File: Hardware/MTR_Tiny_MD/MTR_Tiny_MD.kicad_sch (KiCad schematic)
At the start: 82 parts, among them J1 USB_C_Receptacle_USB2.0, J2 68021-412HLF, J3 LED OUT, J4 UART, J5 LED OUT, J6 XT30PB, Q1 AO3401A, SW1 Boot, SW2 Reset, U1 RP2040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

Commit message: add usb C PD controler
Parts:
- removed C17, C22: 10uF, Capacitor_SMD:C_0603_1608Metric, symbol Device:C
- removed F1: 500mA, Fuse:Fuse_0603_1608Metric, symbol Device:Fuse_Small
- removed F2: 250mA, Fuse:Fuse_0603_1608Metric, symbol Device:Fuse_Small
- removed U4: TPS71933-33DRVR, Personal:TPS71933-33DRVR, symbol 2023-01-28_15-38-30:TPS71933-33DRVR
- added 3v3ToVddd1: 3V3toVddJumper, Resistor_SMD:R_0201_0603Metric, symbol Jumper:SolderJumper_2_Open
- added C14, C16, C19, C22, C43: 4.7uF, Capacitor_SMD:C_0402_1005Metric, symbol Device:C_Small
- added C15, C17, C21: 100nF, Capacitor_SMD:C_0402_1005Metric, symbol Device:C_Small
- added C23: DNF, Capacitor_SMD:C_0402_1005Metric, symbol Device:C_Small
- added Coarse1: CurrentSelect, Resistor_SMD:R_0201_0603Metric, symbol Jumper:SolderJumper_2_Open
- added D4: SAFE_MODE, LED_SMD:LED_0603_1608Metric, symbol Device:LED_Small
- added JP7: +5V_SAFE, Resistor_SMD:R_0201_0603Metric, symbol Jumper:SolderJumper_2_Open
- added JP8: +VBUS_OUT, Resistor_SMD:R_0201_0603Metric, symbol Jumper:SolderJumper_2_Open
- added R10, R24: 20k, Resistor_SMD:R_0402_1005Metric, symbol Device:R_Small
- added R17, R26: 2k2, Resistor_SMD:R_0402_1005Metric, symbol Device:R_Small
- added R18: 820R, Resistor_SMD:R_0402_1005Metric, symbol Device:R_Small
- added R22: 1k, Resistor_SMD:R_0402_1005Metric, symbol Device:R_Small
- added R23: 5.1k, Resistor_SMD:R_0402_1005Metric, symbol Device:R_Small
- added U4, U9: SIA931DJ-T1-GE3, footprints:MOSFET_T1-GE3_VIS, symbol 2023-08-24_16-54-04:SIA931DJ-T1-GE3
- added U8: CYPD3177-24LQXQT, CYPD3177-24LQXQT_CYP, symbol 2023-08-24_13-49-11:CYPD3177-24LQXQT
- added Vbus1, VbusSafe1: VbusJumper, Resistor_SMD:R_0201_0603Metric, symbol Jumper:SolderJumper_2_Open
- added VbusMax1: VbusMax, Resistor_SMD:R_0201_0603Metric, symbol Jumper:SolderJumper_2_Open
- added VbusMin1: VbusMin, Resistor_SMD:R_0201_0603Metric, symbol Jumper:SolderJumper_2_Open
- D3: value USB ON -> LED
- H6, H7: footprint TestPoint:TestPoint_Pad_1.5x1.5mm -> TestPoint:TestPoint_Pad_D1.0mm
- J6: footprint Personal:XT30PB -> footprints:CONN_XT30UPB-M_AMA
- R16: value 100R -> 5.1k
- R5: value 1k -> DNF
- SW1, SW2: footprint Personal:TVBM17 -> Button_Switch_additional:TVAF06-A020B-R
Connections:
- net FeedBack is gone; now on net +3V3: C40.1, C41.1, C42.1, L2.2, U7.4 (FB/VOUT)
- net V_USB is gone; now on net GPIO23: J2.3, R12.2
- net +3V3: now also 3v3ToVddd1.1 (A), Coarse1.1 (A), R23.2, VbusMax1.1 (A)
- net ALIM: now also JP7.2 (B), JP8.2 (B)
- net GND: now also C14.2, C15.2, C16.2, C17.2, C19.1, C21.1, D4.1 (K), R22.1, U8.19 (GND), VbusMin1.1 (A); no longer J1.S1 (SHIELD), U5.41 (EPAD)
- net GPIO24: now also J2.9; no longer J2.7
- net GPIO25: now also J2.7; no longer J2.5
- net I2C_SCL: now also U8.13 (HPI_SCL)
- net I2C_SDA: now also U8.12 (HPI_SDA)
- net USB_D+: no longer J1.A6 (D+)
- net USB_D-: no longer J1.A7 (D-)
- net GPIO23: now reaches U1.35 (GPIO23)
- net +VBUS: now reaches J1.A4 (VBUS), J1.A9 (VBUS), J1.B4 (VBUS), J1.B9 (VBUS)
- net +VBUS: now also C19.2, C21.2, U8.18 (VBUS_IN), Vbus1.1 (A), VbusSafe1.1 (A)
- net CC1: now reaches J1.A5 (CC1)
- net CC1: now also U8.15 (CC1)
- net CC2: now reaches J1.B5 (CC2)
- net CC2: now also U8.14 (CC2)
- new net: D4.2 (A), R18.1
- new net +5V_SAFE: JP7.1 (A), R18.2, U4.3 (D2), U4.8 (D2)
- new net +VBUS_FET_EN: R26.1, U8.3 (VBUS_FET_EN)
- new net +VBUS_OUT: C23.1, J2.5, JP8.1 (A), U8.11 (VDC_OUT), U9.3 (D2), U9.8 (D2)
- new net DRAIN_1: C22.1, R24.2, U9.6 (D1), U9.7 (D1), Vbus1.2 (B)
- new net DRAIN_1_SAFE: C43.1, R10.2, U4.6 (D1), U4.7 (D1), VbusSafe1.2 (B)
- new net GATE: C22.2, C23.2, R24.1, R26.2, U9.2 (G1), U9.5 (G2)
- new net GATE_SAFE: C43.2, R10.1, R17.2, U4.2 (G1), U4.5 (G2)
- new net ISNK_COARSE: Coarse1.2 (B), U8.5 (ISNK_COARSE)
- new net ISNK_FINE: R22.2, R23.1, U8.6 (ISNK_FINE)
- new net SAFE_PWR_EN: R17.1, U8.4 (SAFE_PWR_EN)
- new net SOURCE: U9.1 (S1), U9.4 (S2)
- new net SOURCE_SAFE: U4.1 (S1), U4.4 (S2)
- new net VBUS_MAX: U8.2 (VBUS_MAX), VbusMax1.2 (B)
- new net VBUS_MIN: U8.1 (VBUS_MIN), VbusMin1.2 (B)
- new net VCCD: C16.1, U8.24 (VCCD)
- new net VDDD: 3v3ToVddd1.2 (B), C14.1, C15.1, C17.1, U8.23 (VDDD)
- no-connect marks 10 -> 14
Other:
- note added: "DNF - Not on PCB"
- note added: "Fine current +/-250mA"
- note added: "Maximal voltage 20V"
- note added: "Minimun voltage 5V"
- note added: "Nominal current 0-5A"
- note added: "Safe 5V feedback if negociation fail"
- note added: "USB C + Power Delivery"
- note removed: "USB C + Power"
- moved on the sheet: C1, C10, C11, C12, C13, C18, C20, C24, C25, C26, C27, C28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

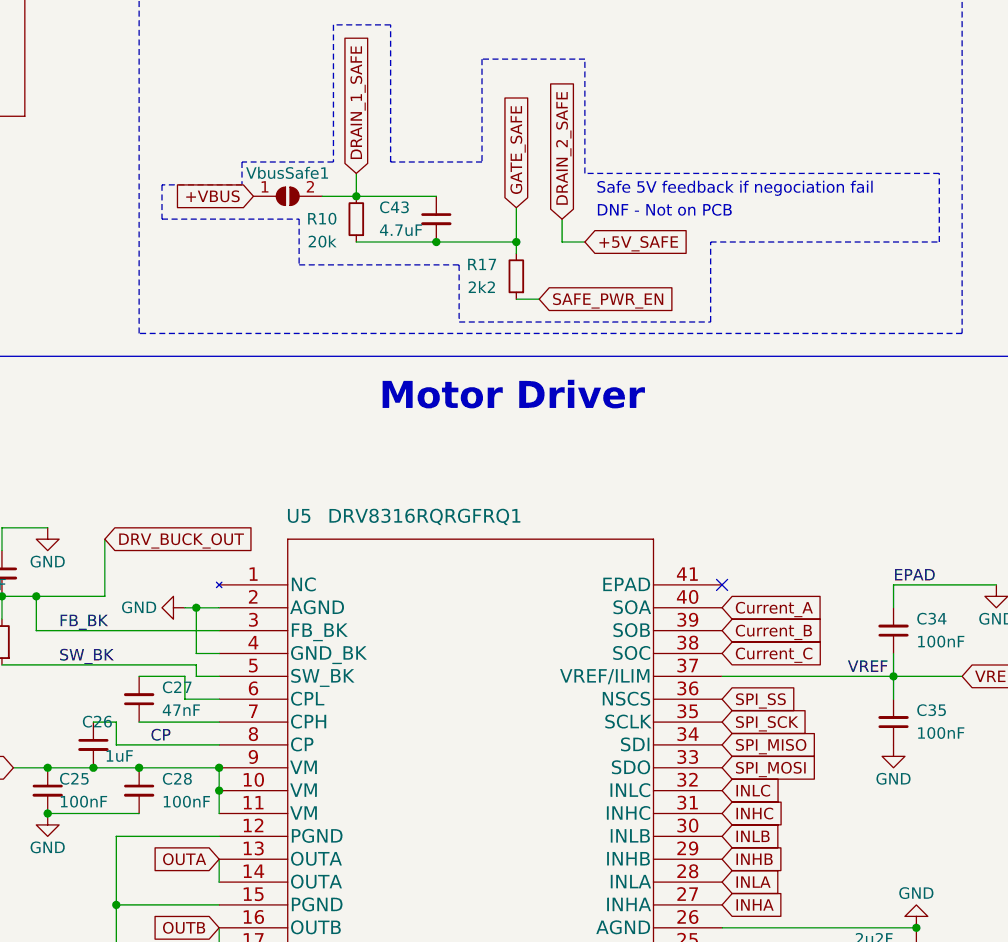
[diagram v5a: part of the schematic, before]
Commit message: Update design, add PD controler, correct SPI
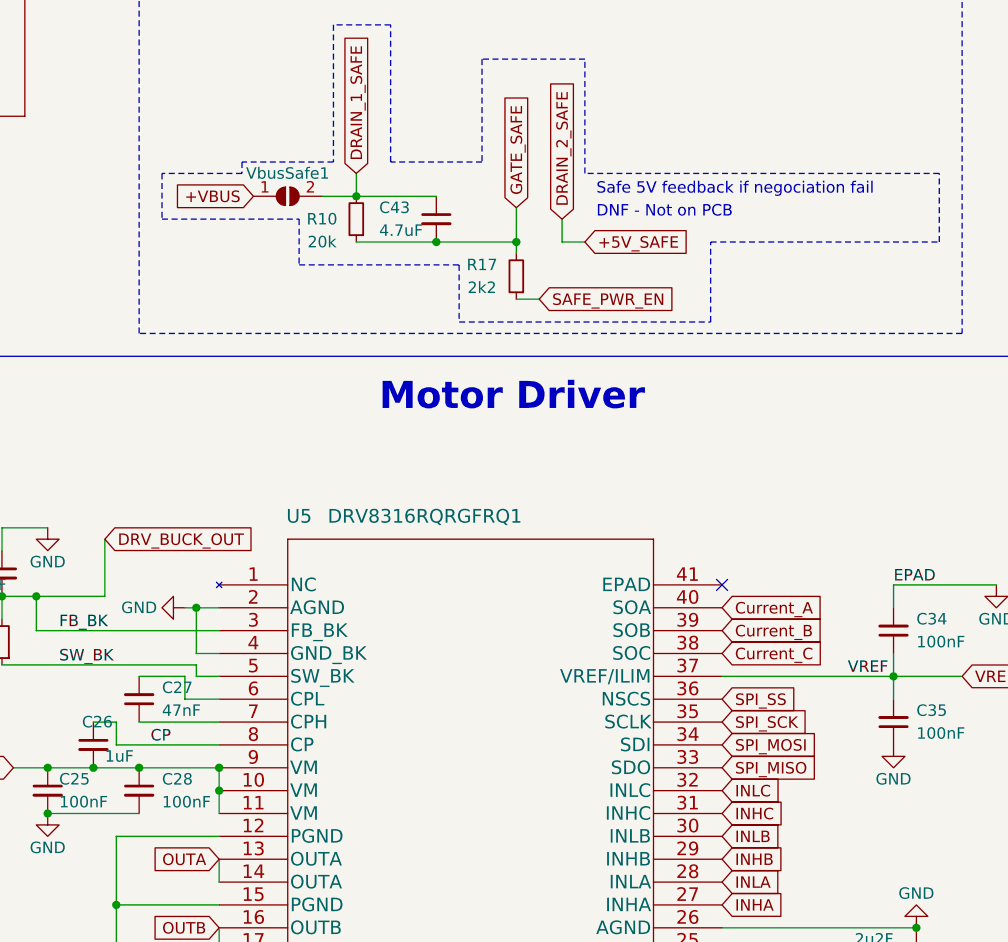
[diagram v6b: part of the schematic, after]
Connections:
- net SPI_MISO: now also U5.33 (SDO); no longer U5.34 (SDI)
- net SPI_MOSI: now also U5.34 (SDI); no longer U5.33 (SDO)

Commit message: Update 1.2.2
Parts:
- added C44: 2u2, Capacitor_SMD:C_0402_1005Metric, symbol Device:C_Small
- added R19: 5.1k, Resistor_SMD:R_0402_1005Metric, symbol Device:R_Small
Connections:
- net +3V3: now also R19.1
- net GND: now also C44.1
- net RUN: now also C44.2, R19.2
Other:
- note added: "16MB QSPI Flash"
- note added: "Boot button"
- note removed: "8MB QSPI Flash"
- note removed: "Force Flash boot"
- moved on the sheet: C18, C20, R4, R5, R9, SW1, SW2, U2
